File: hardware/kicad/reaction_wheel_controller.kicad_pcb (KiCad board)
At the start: 4 copper layers, 90 x 70 mm, 86 parts, among them J1 5V INPUT: 1=+5V 2=GND, J2 SWD: VTref IO GND CLK RST SWO, J3 CAN: H L GND, J4 TERM: shunt=ON, J5 ENC: 3V3 GND A B Z, J6 ESC: PWM EN FAULT GND TX RX, J7 DEBUG: TX RX GND, U1 STM32G431RBT6, U2 AP2112K-3.3TRG1, U3 TCAN3413DR, U4 LSM6DSLTR, U5 SN74LVC1G126DBVR

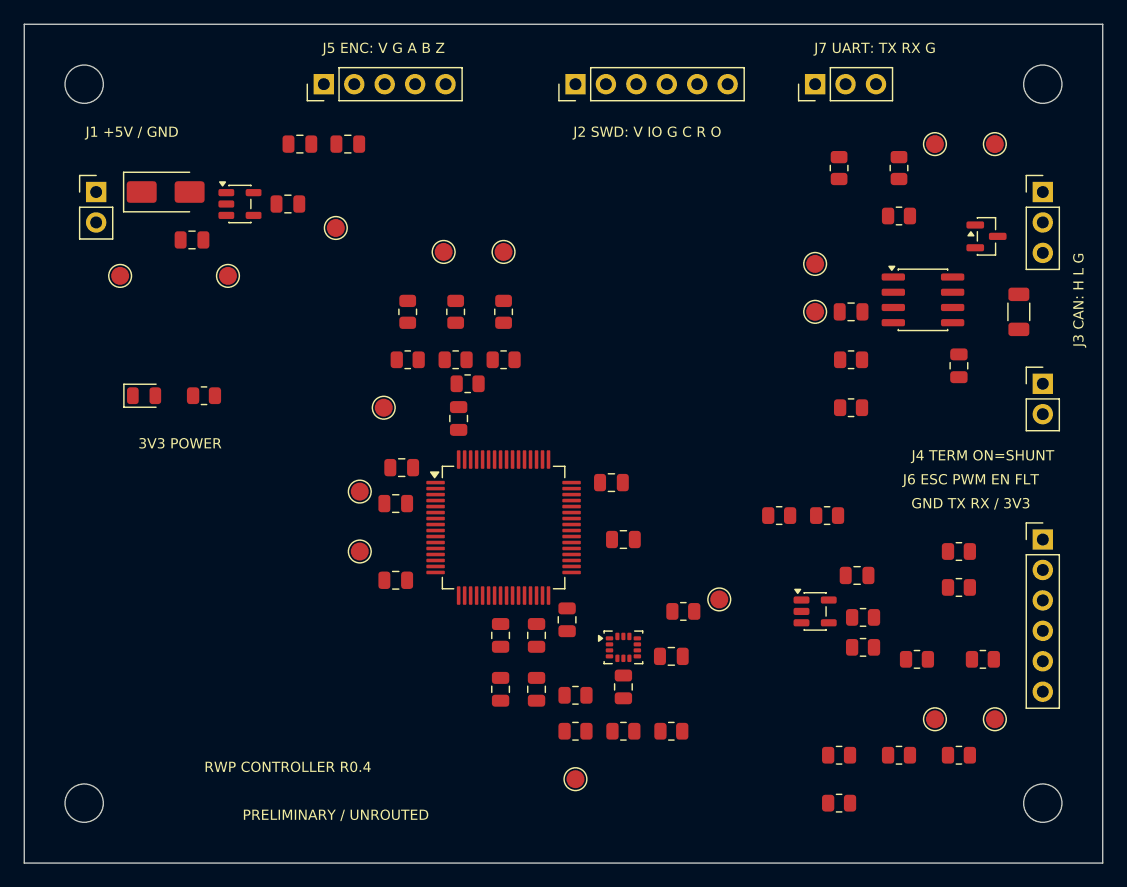
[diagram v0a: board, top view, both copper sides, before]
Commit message: hardware: route power and ground checkpoint
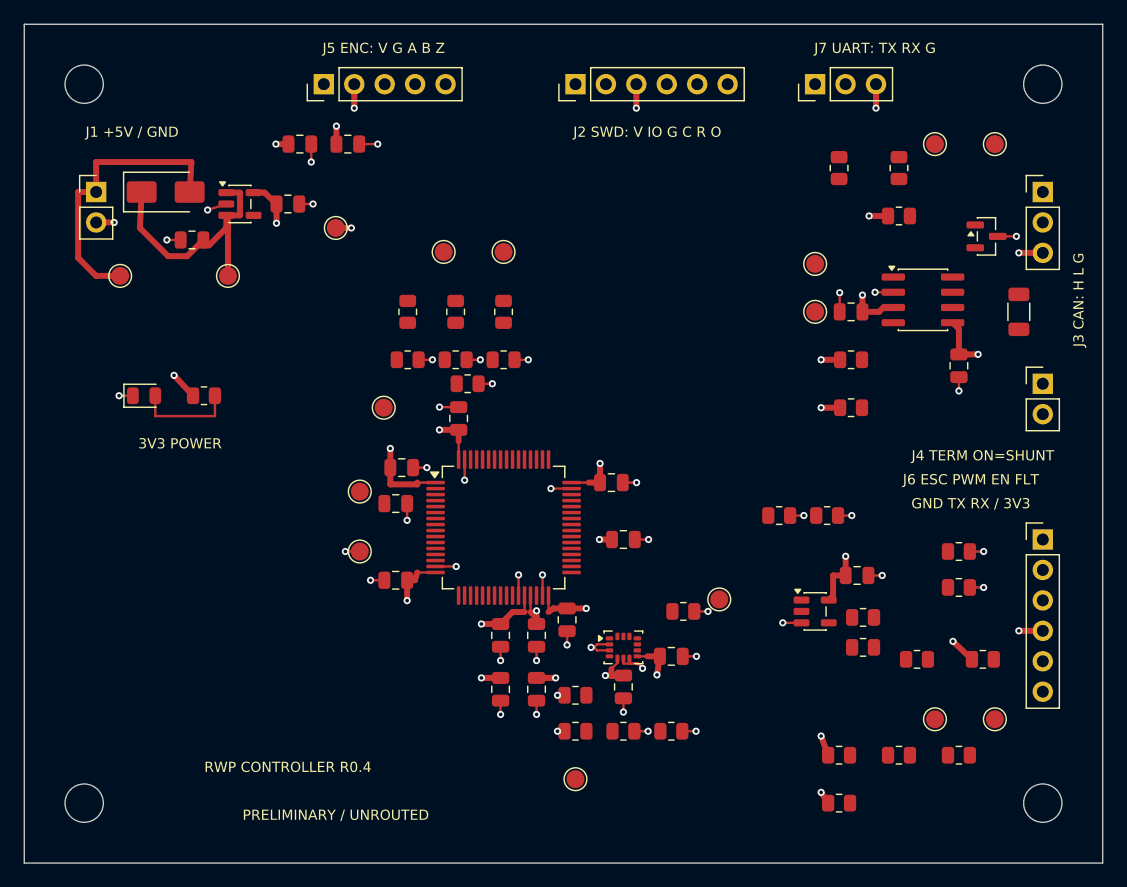
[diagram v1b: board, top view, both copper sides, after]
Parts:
- turned C1 to 180 degrees
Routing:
- net +3V3: track 0.00 -> 79.5 mm, vias 0 -> 28
- net GND: track 0.00 -> 73.5 mm, vias 0 -> 50
- net /MCU POWER SWD/+5V_IN: track 0.00 -> 24.1 mm
- net /MCU POWER SWD/+5V_PROTECTED: track 0.00 -> 23.1 mm
- net /MCU POWER SWD/LED_A: track 0.00 -> 8.38 mm
- added copper zone on In2.Cu, net +3V3
- added copper zone on In1.Cu, net GND

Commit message: hardware: record CAN routing and incomplete IMU draft
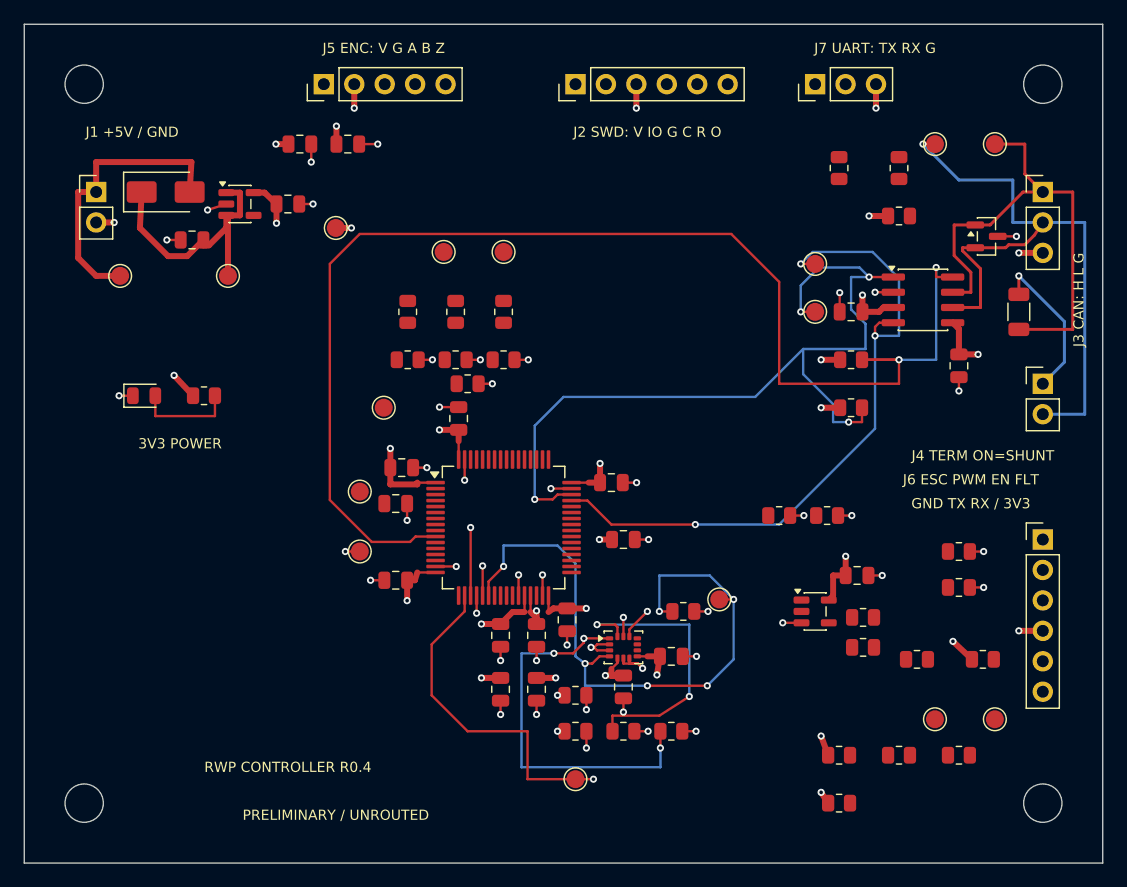
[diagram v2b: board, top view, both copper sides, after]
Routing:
- net CAN_STB: track 0.00 -> 110.0 mm, vias 0 -> 2
- net FDCAN_TX: track 0.00 -> 70.5 mm, vias 0 -> 4
- net IMU_CS_N: track 0.00 -> 57.6 mm, vias 0 -> 3
- net FDCAN_RX: track 0.00 -> 57.2 mm, vias 0 -> 3
- net IMU_INT1: track 0.00 -> 54.8 mm, vias 0 -> 6
- net /CAN IMU/CANL: track 0.00 -> 54.4 mm, vias 0 -> 1
- net IMU_MISO: track 0.00 -> 45.1 mm, vias 0 -> 4
- net IMU_MOSI: track 0.00 -> 42.6 mm, vias 0 -> 3
- net /CAN IMU/CANH: track 0.00 -> 41.8 mm
- net IMU_SCK: track 0.00 -> 39.7 mm, vias 0 -> 3
- net /CAN IMU/CAN_TERM: track 0.00 -> 12.9 mm, vias 0 -> 1

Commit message: hardware: complete controller routing and native DRC
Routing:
- net ESC_UART_RX: track 0.00 -> 75.7 mm, vias 0 -> 4
- net /MCU POWER SWD/NRST: track 0.00 -> 75.2 mm, vias 0 -> 3
- net ESC_UART_TX: track 0.00 -> 69.1 mm, vias 0 -> 3
- net ESC_FAULT_N: track 0.00 -> 66.8 mm, vias 0 -> 2
- net UART_RX: track 0.00 -> 64.6 mm, vias 0 -> 2
- net /MCU POWER SWD/SWO: track 0.00 -> 54.8 mm, vias 0 -> 1
- net ESC_ENABLE: track 0.00 -> 49.3 mm, vias 0 -> 5
- net /MCU POWER SWD/SWCLK: track 0.00 -> 46.0 mm, vias 0 -> 1
- net UART_TX: track 0.00 -> 45.6 mm, vias 0 -> 2
- net /ENCODER ESC/ESC_PWM: track 0.00 -> 41.6 mm, vias 0 -> 2
- net /MCU POWER SWD/SWDIO: track 0.00 -> 33.3 mm, vias 0 -> 1
- net ENC_B: track 0.00 -> 32.7 mm, vias 0 -> 3
- net MOTOR_PWM: track 0.00 -> 31.5 mm, vias 0 -> 3
- net /ENCODER ESC/ESC_EN_OUT: track 0.00 -> 28.6 mm, vias 0 -> 3
- net ENC_Z: track 0.00 -> 27.9 mm, vias 0 -> 2
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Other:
- board text added: "+Z OUT / U4 ROT0"
- board text added: "IMU +X > +Y UP"
- board text added: "IMU native +X right / +Y upper / +Z out; U4 rotation0; mechanical transform TBD"
- board text added: "ROUTED / NOT RELEASED"
- board text added: "RWP CONTROLLER R0.5"
- board text removed: "IMU native axes: review DS Fig1"
- board text removed: "PRELIMINARY / UNROUTED"
- board text removed: "RWP CONTROLLER R0.4"
